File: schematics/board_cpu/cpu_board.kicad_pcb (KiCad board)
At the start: 2 copper layers, 150.3 x 100.3 mm, 66 parts, among them J600 Euro96pin, J601 clock, J602 clock1, J602_1 clock_dtack, J603 Conn_02x08_Counter_Clockwise, J604 systemTickFreq, J605 Conn_01x32, Q7 2N3904, Q8 2N3904, SW1 Reset, U600 68000D, U600rst1 ICM7555xB, U601 74LS393, U602 74HC164, U603 74HC14, U604 ATmega8-16P, U605 74LS20, U606 74HC4078, U607 74LS139

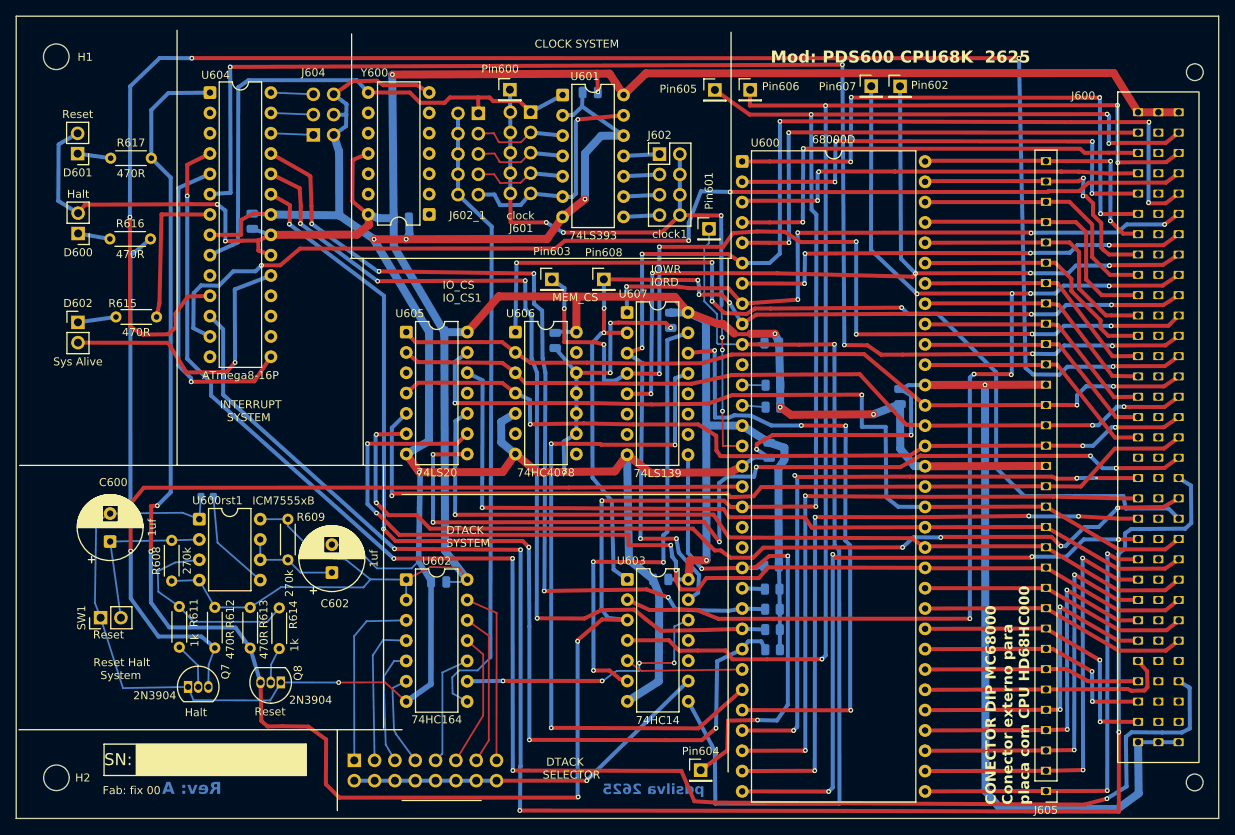
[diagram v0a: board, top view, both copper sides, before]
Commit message: Finished PDS100 routing
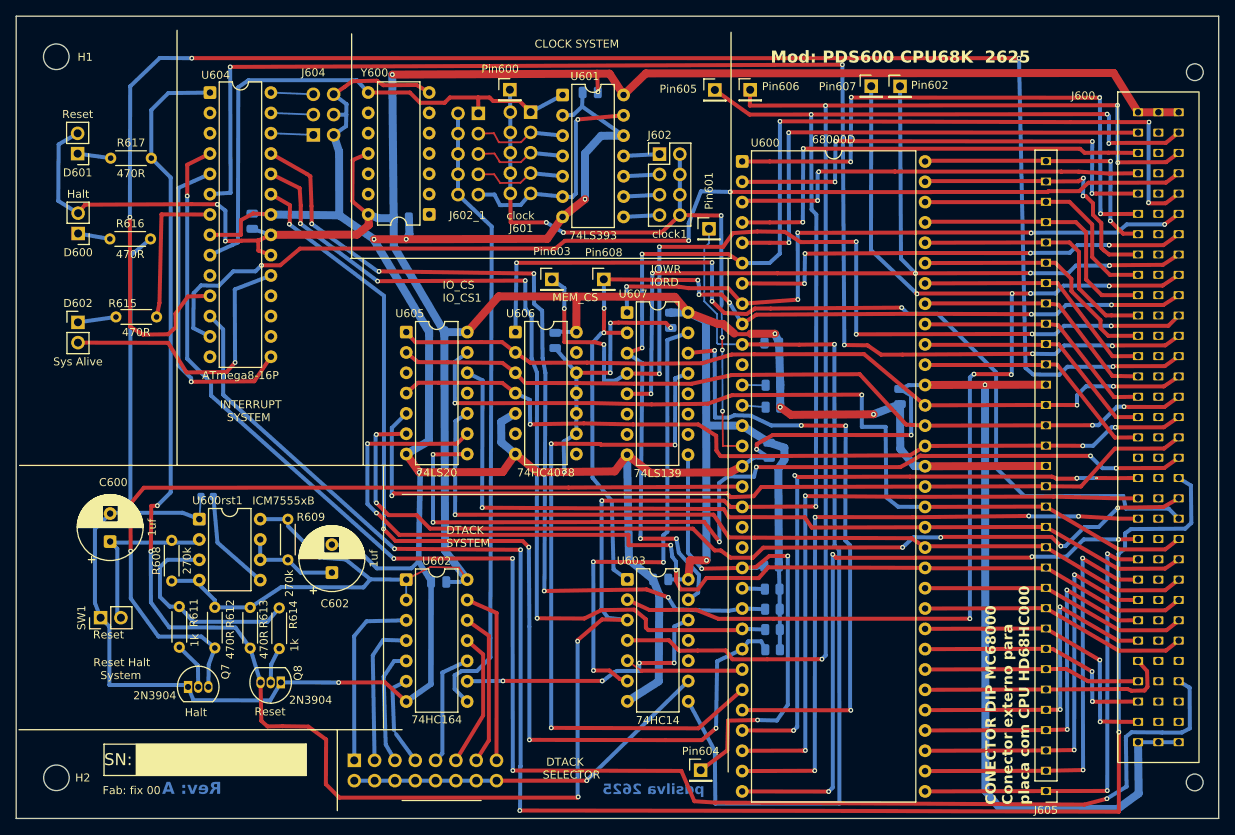
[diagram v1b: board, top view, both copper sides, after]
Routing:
- net GND: track 518.5 -> 519.8 mm
- net Net-(SW1-Pin_2): track 20.8 -> 21.7 mm
- net //IPL1: track 111.4 -> 112.1 mm
- net Net-(U600rst1-Q): track 25.4 -> 26.1 mm
- net Net-(J602_1-Pin_10): track 79.7 -> 79.1 mm

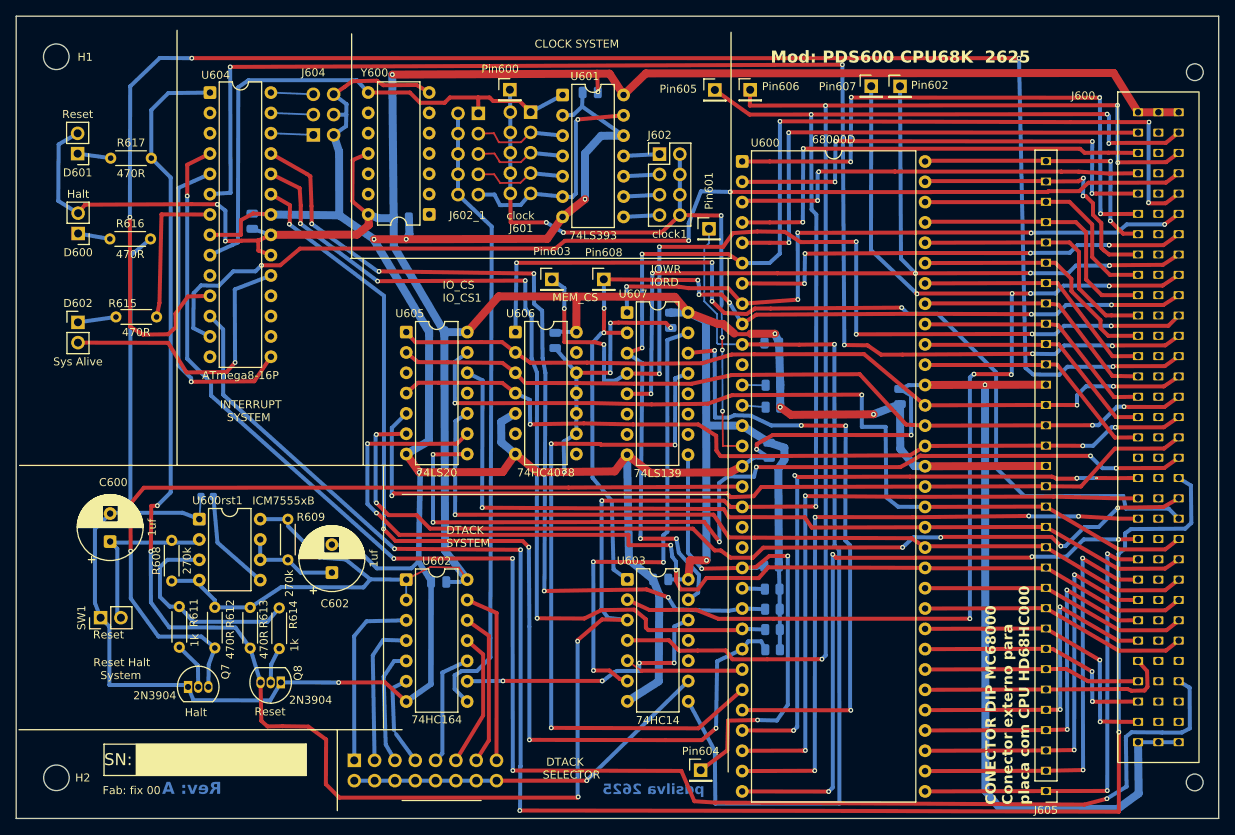
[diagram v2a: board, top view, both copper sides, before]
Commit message: Finished PDS100 routing
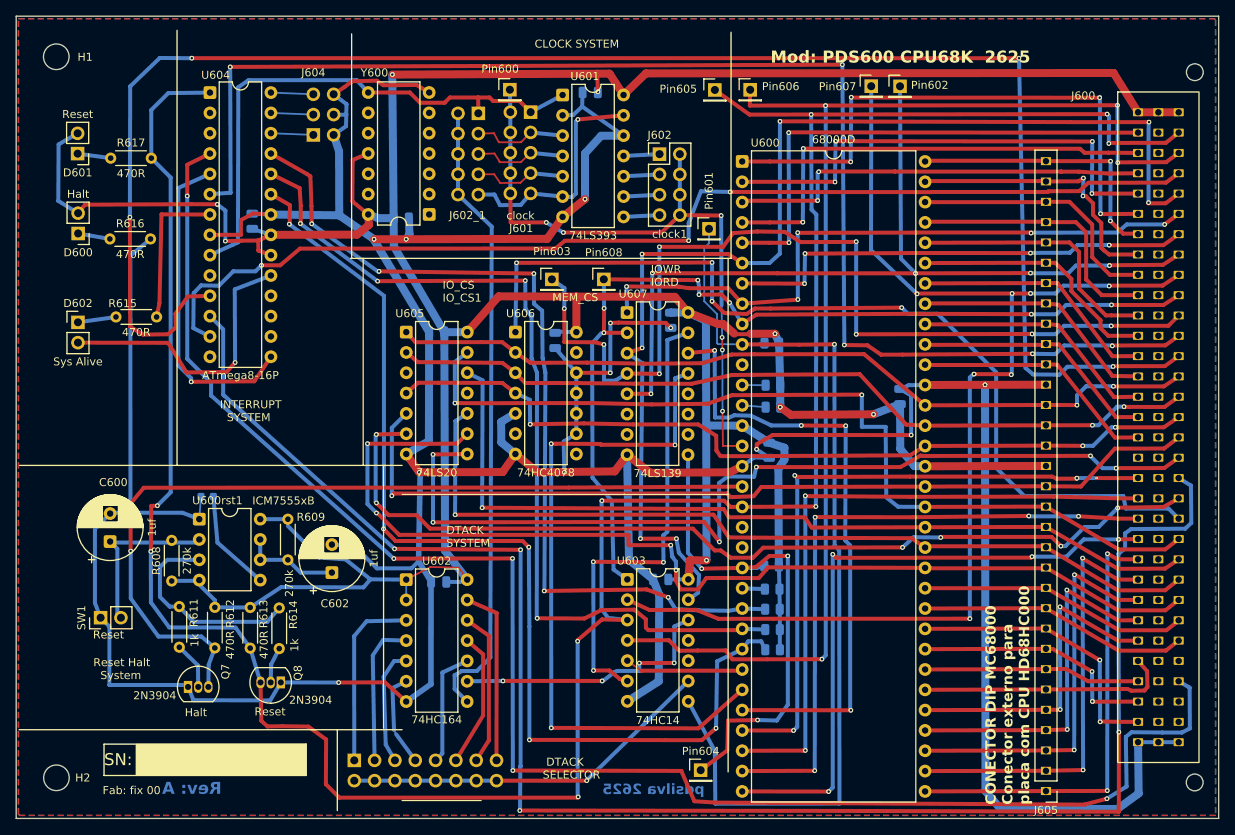
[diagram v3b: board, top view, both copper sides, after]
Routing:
- added copper zone on F.Cu, net +5V
- added copper zone on B.Cu, net GND
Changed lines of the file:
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@@
 		(net 171)
+	)
+	(zone
+		(net 5)
+		(net_name "+5V")
+		(layer "F.Cu")
+		(hatch edge 0.5)
+		(priority 1)
+		(connect_pads
+			(clearance 0.5)
+		)
+		(min_thickness 0.25)
+		(filled_areas_thickness no)
+		(fill yes
+			(thermal_gap 0.5)
+			(thermal_bridge_width 0.5)
+		)
+		(polygon
+			(pts
+				(xy 119.979 29.284) (xy 269.465 29.284) (xy 269.597 29.416) (xy 269.597 128.861) (xy 120.125 128.861)
+				(xy 119.979 128.715)
+			)
+		)
+	)
+	(zone
+		(net 1)
+		(net_name "GND")
+		(layer "B.Cu")
+		(hatch edge 0.5)
+		(connect_pads
+			(clearance 0.5)
+		)
+		(min_thickness 0.25)
+		(filled_areas_thickness no)
+		(fill yes
+			(thermal_gap 0.5)
+			(thermal_bridge_width 0.5)
+		)
+		(polygon
+			(pts
+				(xy 119.977 29.282) (xy 269.465 29.282) (xy 269.597 29.414) (xy 269.597 128.861) (xy 120.125 128.861)
+				(xy 119.937 128.673) (xy 119.937 29.281) (xy 119.976 29.281) (xy 119.979 29.284)
+			)
+		)
 	)
 	(embedded_fonts no)
